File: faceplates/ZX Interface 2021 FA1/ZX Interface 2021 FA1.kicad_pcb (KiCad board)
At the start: 2 copper layers, 87.6 x 92.7 mm, 8 parts, among them M1 Mounting, M2 Mounting, M3 Mounting, M4 Mounting, M5 Mounting, M6 Mounting

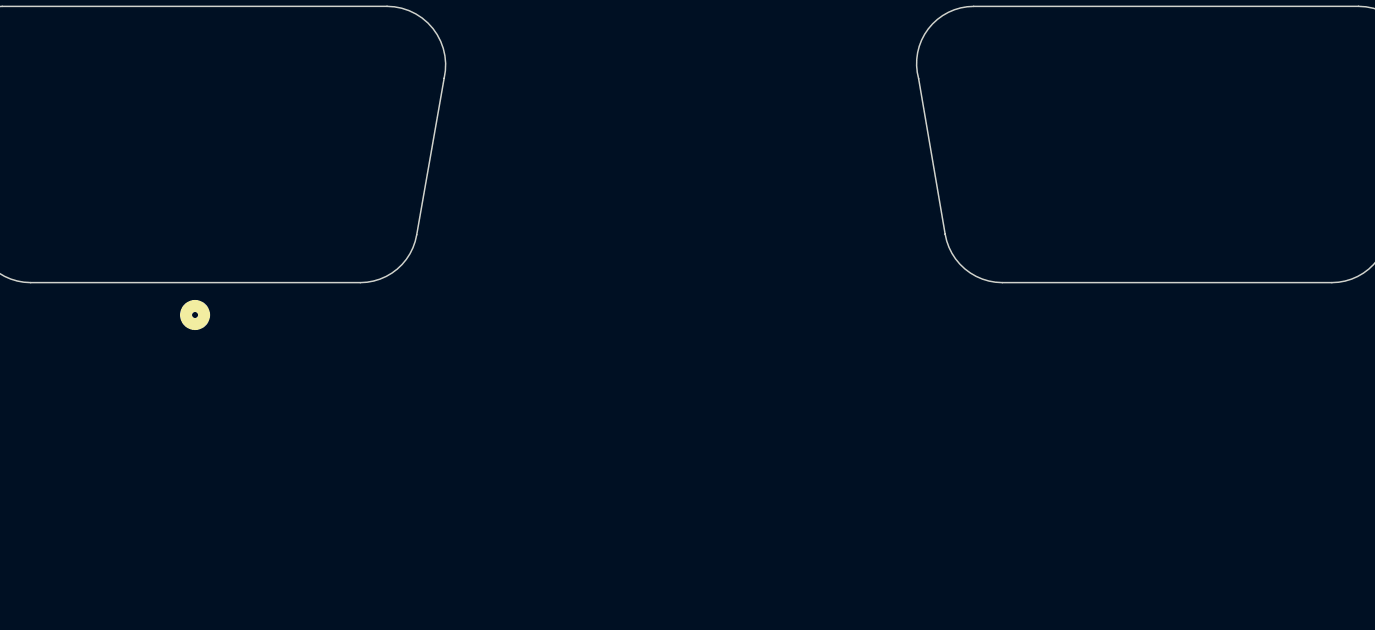
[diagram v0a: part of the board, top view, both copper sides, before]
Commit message: Made 74ls245 open collector instead of using resistors
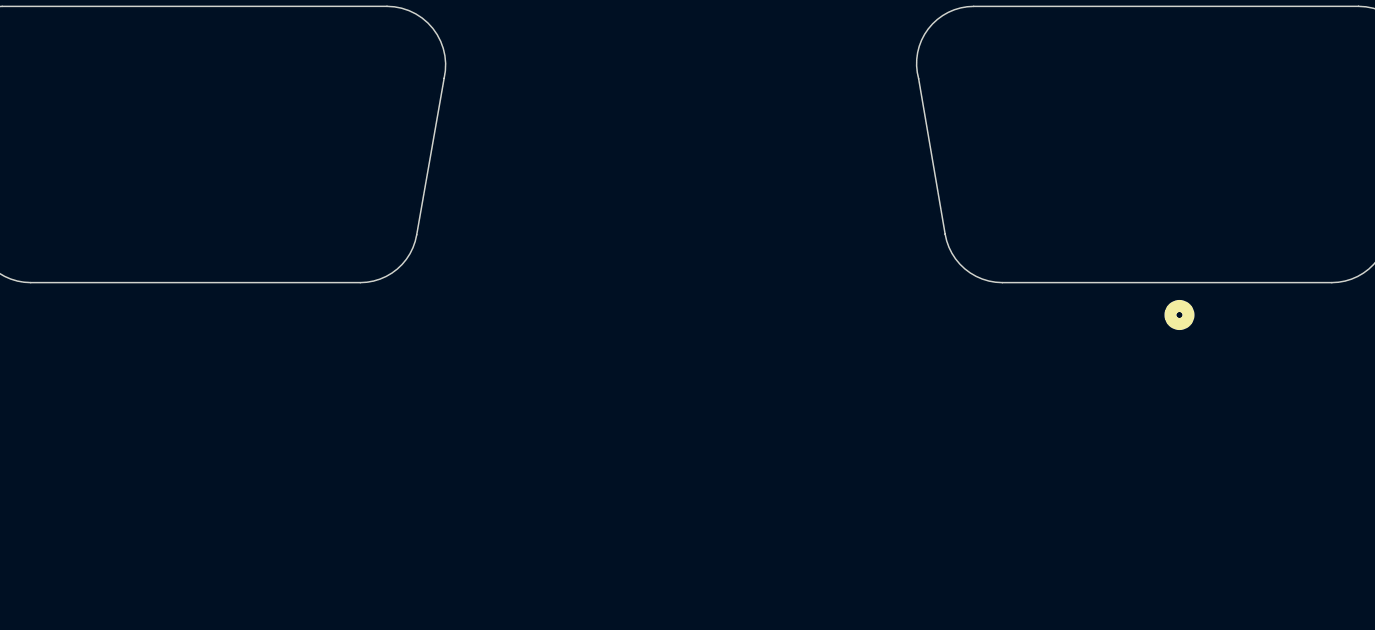
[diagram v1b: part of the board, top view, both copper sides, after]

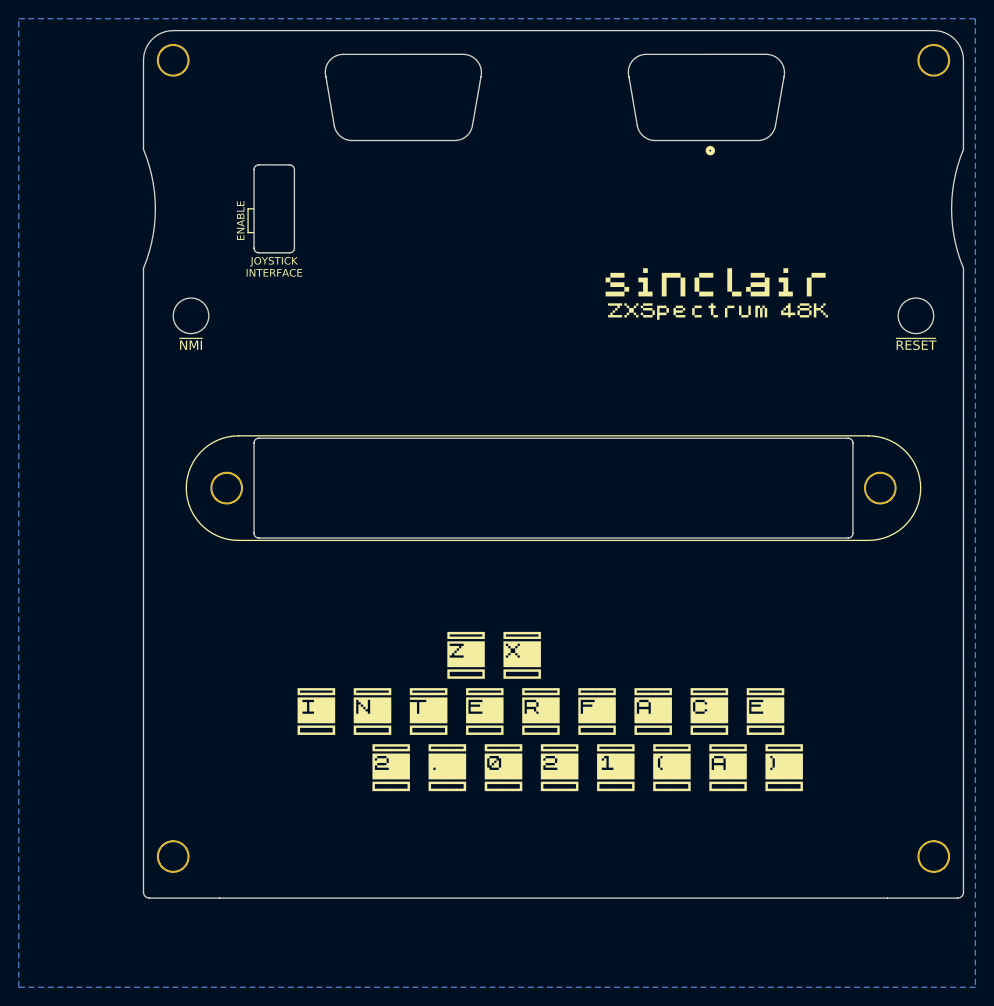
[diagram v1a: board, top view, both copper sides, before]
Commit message: Add POWER LED cutout
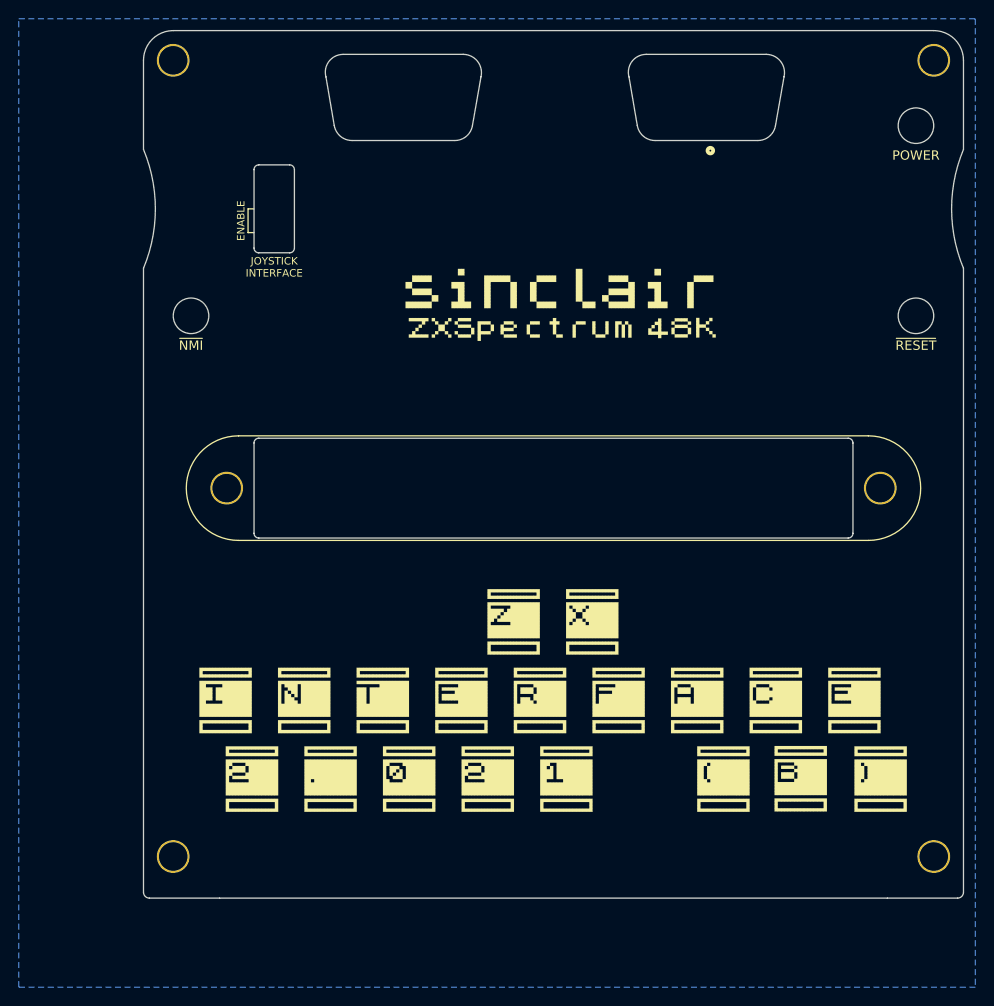
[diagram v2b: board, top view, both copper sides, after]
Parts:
- sinclair_title: footprint artwork:sinclair_title -> artwork:sinclair_title_large
- moved sinclair_title 21.6 mm to (129.5, 71.1)
- moved sinclair_title 12.6 mm to (105.4, 106.0)
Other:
- outline, holes or cut-outs redrawn
- board text added: "POWER"

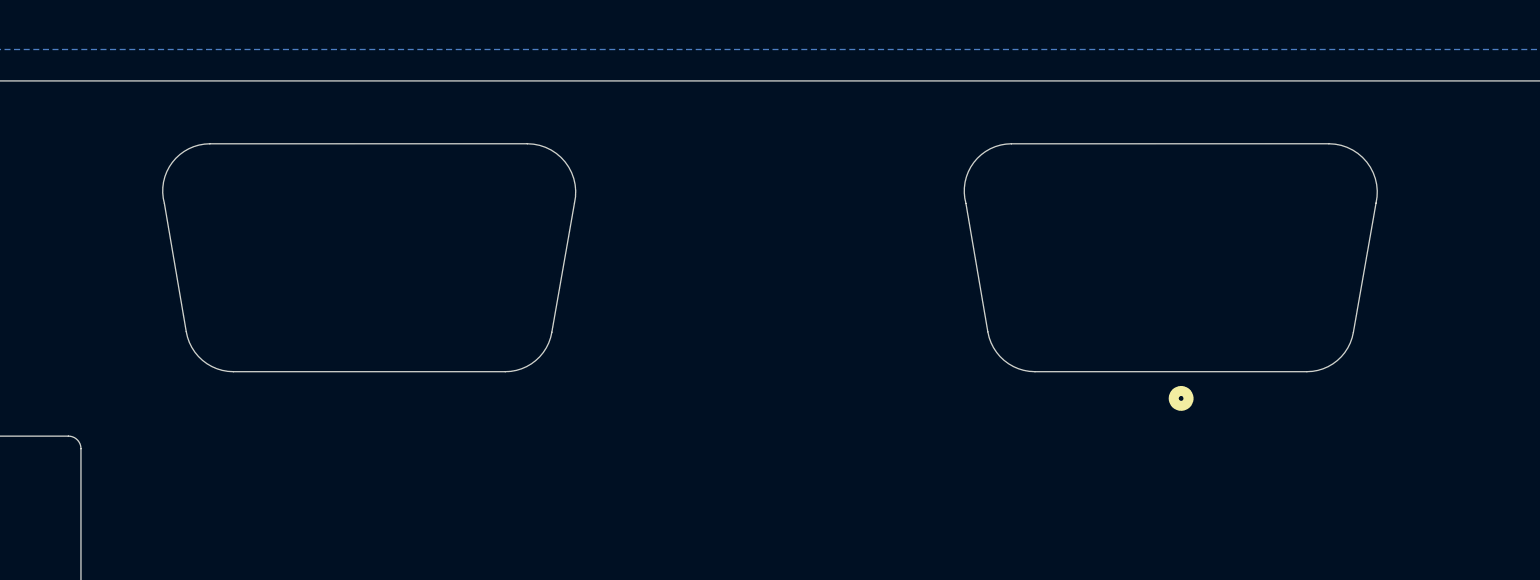
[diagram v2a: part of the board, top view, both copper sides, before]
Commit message: Silkscreen tweaks
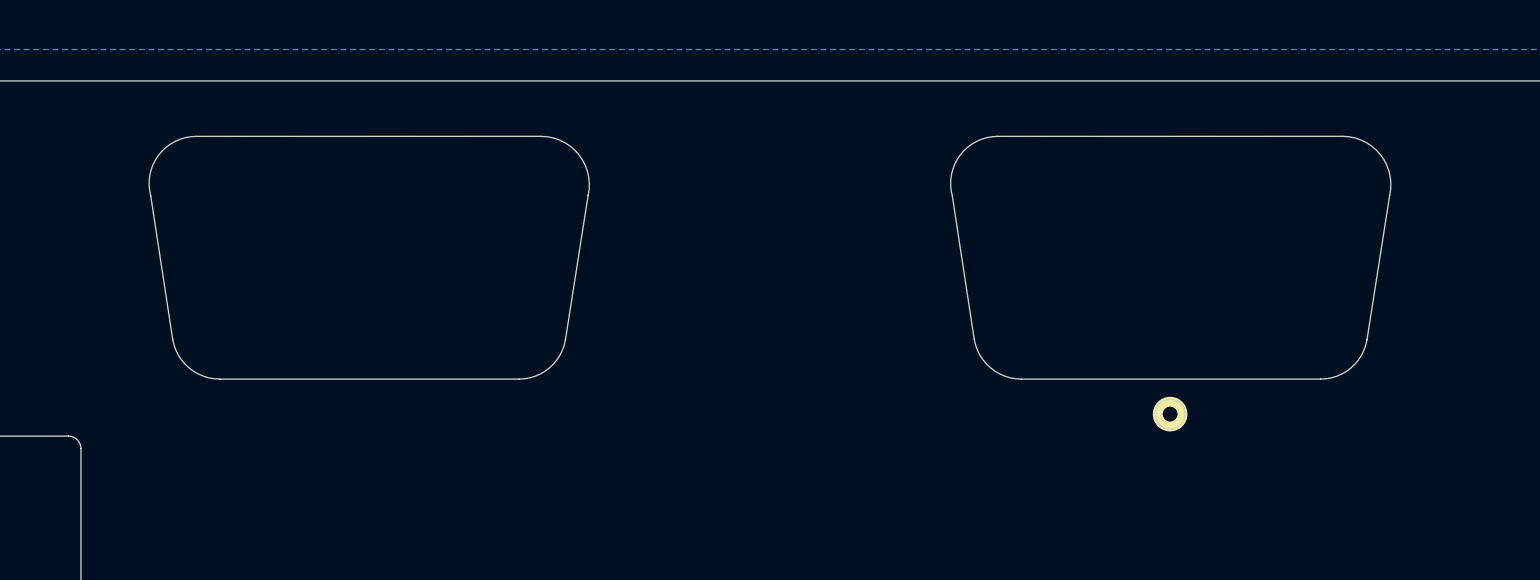
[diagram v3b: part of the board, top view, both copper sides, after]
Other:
- outline, holes or cut-outs redrawn

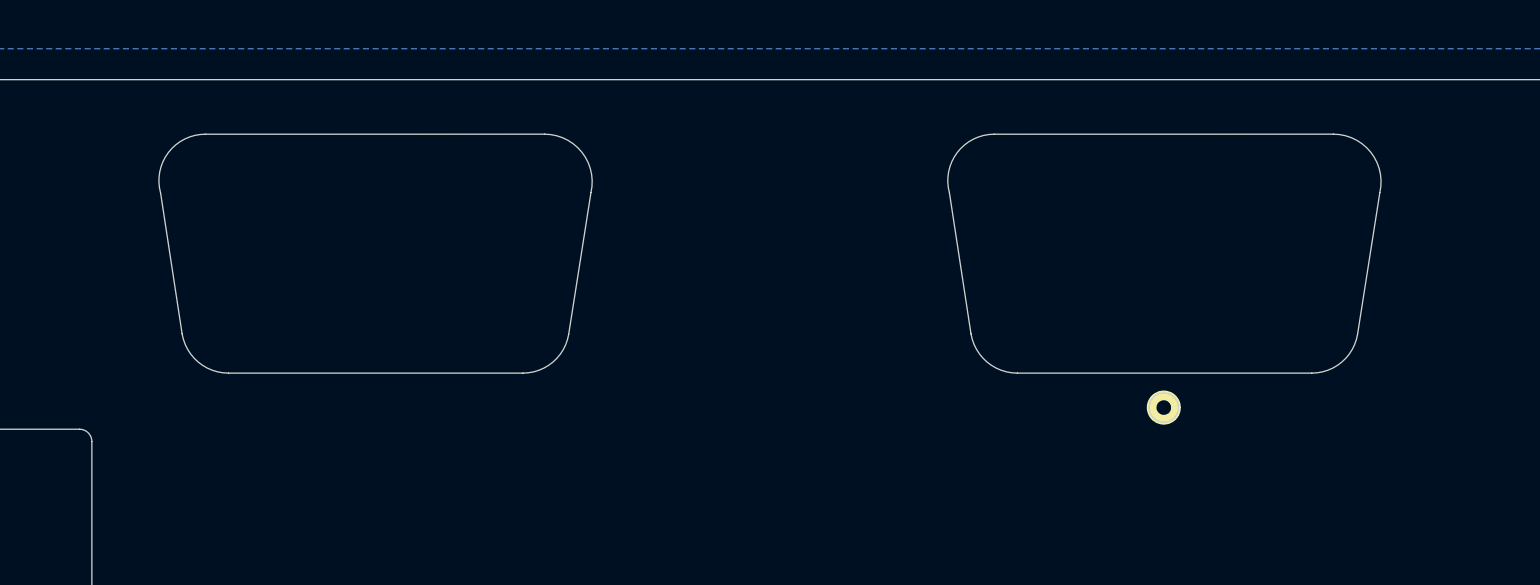
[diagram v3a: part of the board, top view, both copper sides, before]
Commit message: Larger DB9 cutouts
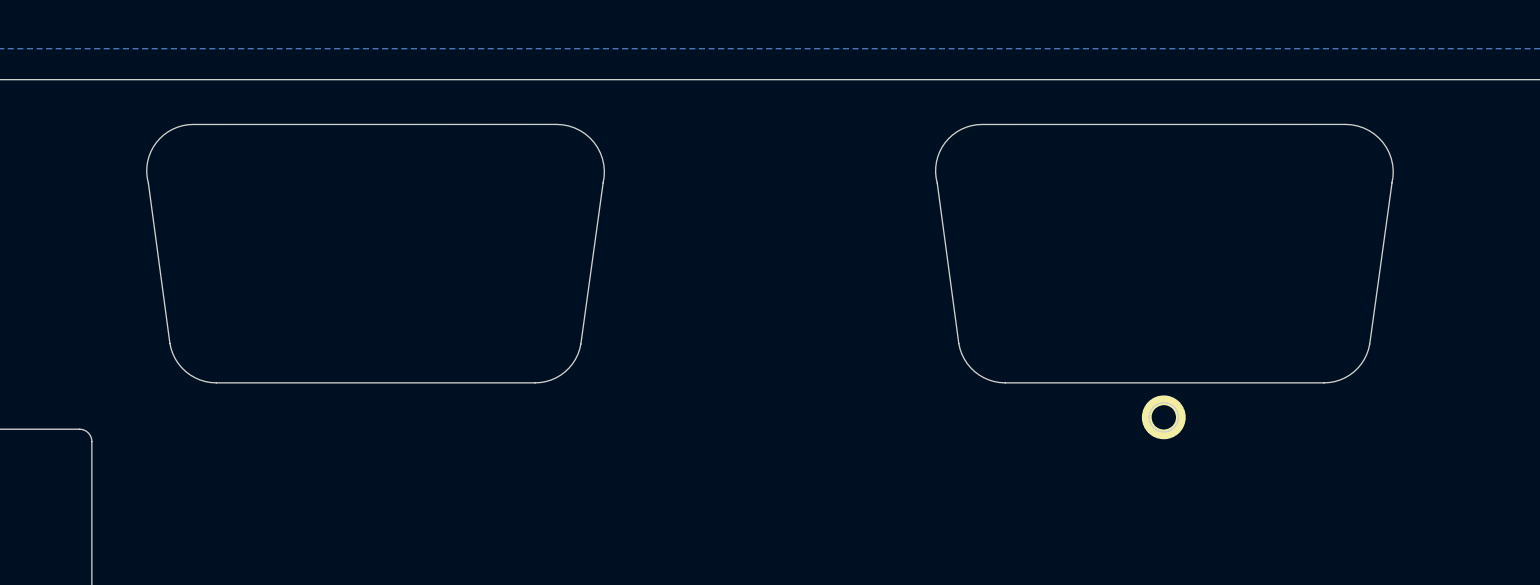
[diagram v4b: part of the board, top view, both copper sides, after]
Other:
- outline, holes or cut-outs redrawn
- board text removed: "USE ONLY WITH ATARI DB9 RANGE OF JOYSTICKS"
